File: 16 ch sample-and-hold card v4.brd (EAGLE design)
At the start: 77.2 x 24.8 mm, 33 parts, among them IC1 TL074D, IC2 TL074D, IC3 TL074D, IC4 TL074D, IC5 DG408DY, IC6 DG408DY

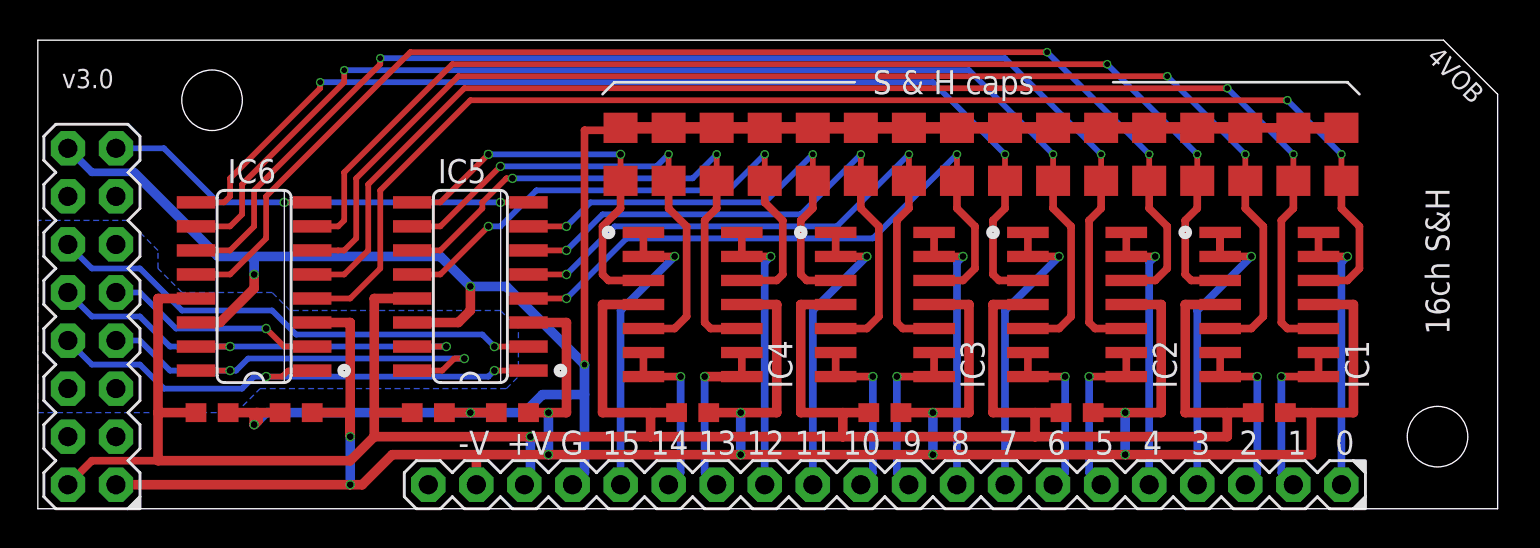
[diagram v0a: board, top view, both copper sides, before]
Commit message: Added new version using 4051 MUX
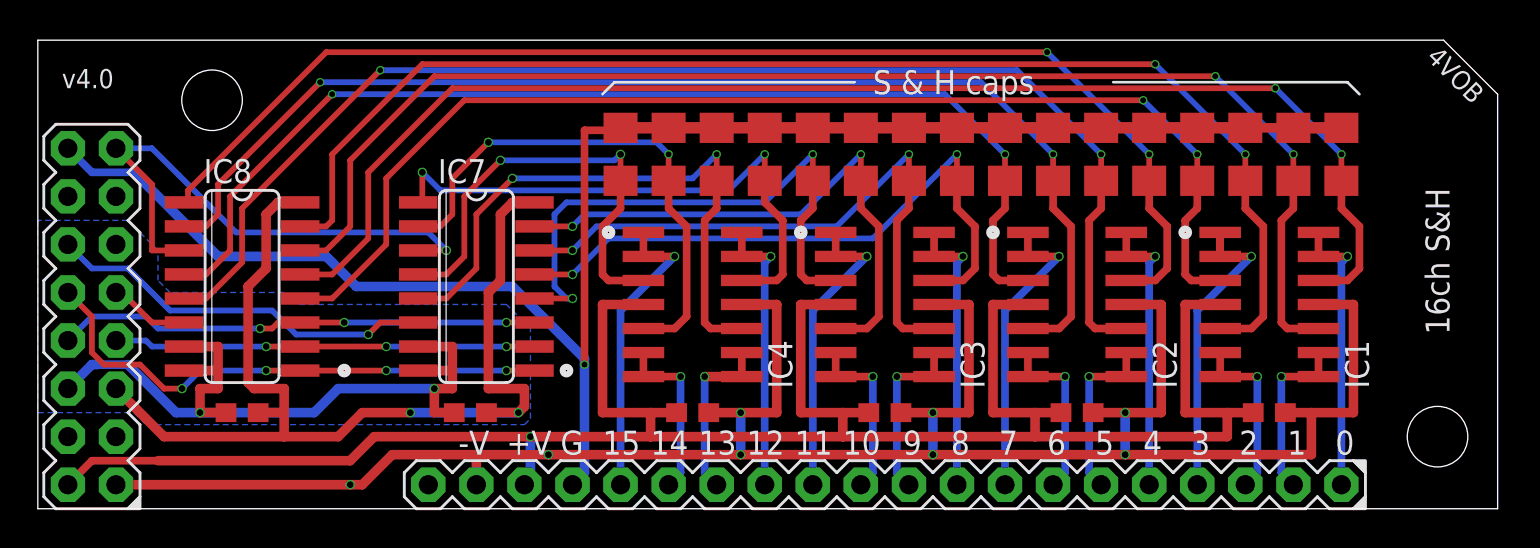
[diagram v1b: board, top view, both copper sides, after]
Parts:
- removed C1, C3: 0.1uF, resistor:C0603
- removed IC5, IC6: DG408DY, maxim:SO16
- added IC7, IC8: 4051D, 40xx:SO16
- moved C2 2.22 mm to (22.5, 5.08), turned to 0 degrees
- moved C40 1.59 mm to (10.5, 5.08), turned to 0 degrees
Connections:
- new net +5V: C2.2, C40.2, IC7.16, IC8.16, SV3.5
- net +15V: no longer C2.2, C40.2, IC5.13, IC6.13
- net -15V: no longer C1.1, C3.1, IC5.3, IC6.3
- net A0: now also IC7.11, IC8.11; no longer IC5.1, IC6.1
- net A1: now also IC7.10, IC8.10; no longer IC5.16, IC6.16
- net A2: now also IC7.9, IC8.9; no longer IC5.15, IC6.15
- net AGND: no longer C1.2, C2.1, C3.2, C40.1, IC5.14, IC6.14
- net DAC: now also IC7.3, IC8.3; no longer IC5.8, IC6.8
- net DGND: now also C2.1, C40.1, IC7.7, IC7.8, IC8.7, IC8.8; no longer SV3.5
- net EN1: now also IC8.6; no longer IC6.2
- net EN2: now also IC7.6; no longer IC5.2
- net IN_0: now also IC8.13; no longer IC6.4
- net IN_1: now also IC8.14; no longer IC6.5
- net IN_10: now also IC7.15; no longer IC5.6
- net IN_11: now also IC7.12; no longer IC5.7
- net IN_12: now also IC7.1; no longer IC5.12
- net IN_13: now also IC7.5; no longer IC5.11
- net IN_14: now also IC7.2; no longer IC5.10
- net IN_15: now also IC7.4; no longer IC5.9
- net IN_2: now also IC8.15; no longer IC6.6
- net IN_3: now also IC8.12; no longer IC6.7
- net IN_4: now also IC8.1; no longer IC6.12
- net IN_5: now also IC8.5; no longer IC6.11
- net IN_6: now also IC8.2; no longer IC6.10
- net IN_7: now also IC8.4; no longer IC6.9
- net IN_8: now also IC7.13; no longer IC5.4
- net IN_9: now also IC7.14; no longer IC5.5
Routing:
- net +5V: track 0.00 -> 56.7 mm, vias 0 -> 2
- net DGND: track 0.00 -> 40.0 mm, vias 0 -> 2
- net AGND: track 126.3 -> 91.3 mm, vias 5 -> 1
- net -15V: track 143.7 -> 118.9 mm, vias 10 -> 8
- net +15V: track 139.2 -> 115.3 mm
- net EN1: track 11.6 -> 4.25 mm, vias 1 -> 0
- net EN2: track 26.6 -> 20.8 mm
- net IN_11: track 25.6 -> 31.0 mm
- net DAC: track 24.5 -> 29.1 mm, vias 2 -> 1
- net A2: track 24.8 -> 28.3 mm, vias 2 -> 4
- net IN_15: track 21.1 -> 24.2 mm
- net A0: track 28.4 -> 25.6 mm, vias 2 -> 3
- net IN_7: track 56.3 -> 58.9 mm
- net IN_13: track 29.8 -> 32.0 mm
- net A1: track 24.2 -> 22.3 mm, vias 2 -> 3
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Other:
- board text added: "v4.0"
- board text removed: "DGND"
- board text removed: "v3.0"

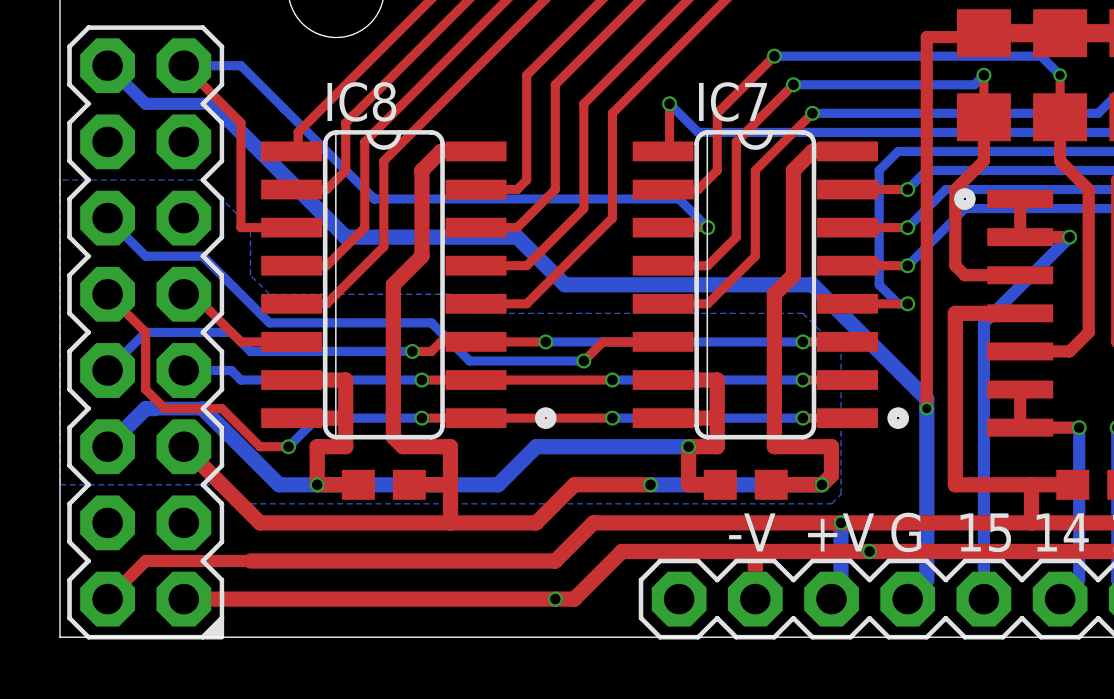
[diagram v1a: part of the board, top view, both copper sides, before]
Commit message: Added 5v reg for muxes directly on board
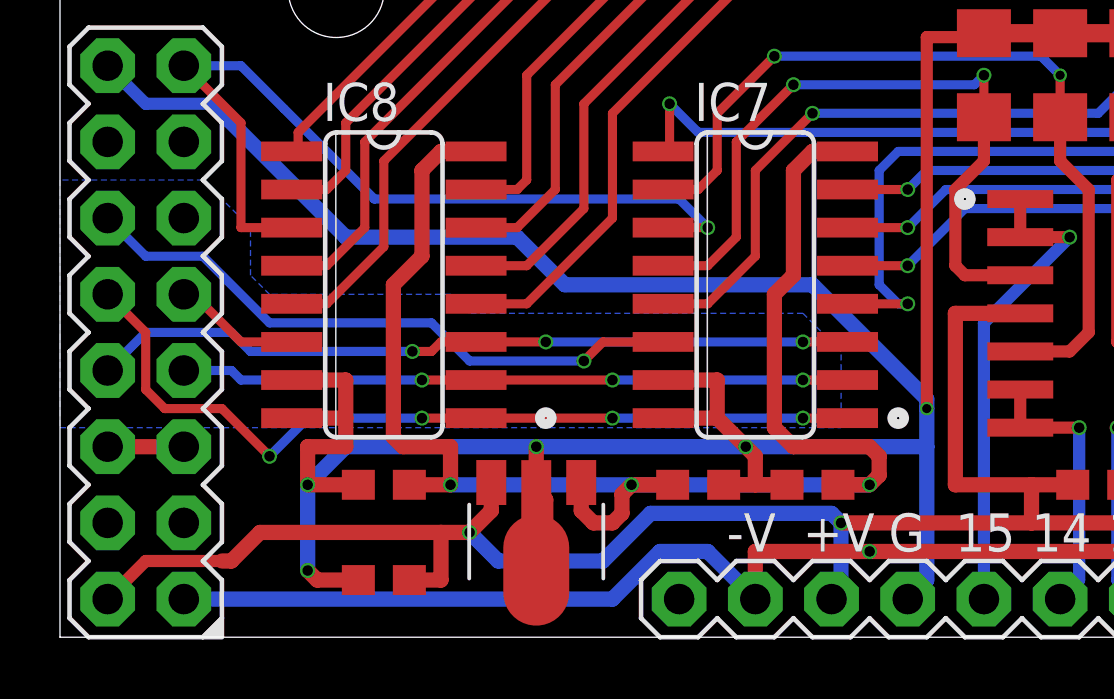
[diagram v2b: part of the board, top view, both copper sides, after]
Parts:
- added C1: 0.1uF, resistor:C0603
- added C3: 0.33uF, resistor:C0603
- added IC5: 78L05F, linear:SOT89
- moved C2 2.22 mm to (24.8, 5.08)
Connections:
- net +15V: now also C3.2, IC5.3
- net +5V: now also C1.2, IC5.1; no longer SV3.5
- net AGND: now also C1.1, C2.1, C3.1, C40.1, IC5.2, IC5.2@1, IC7.7, IC7.8, IC8.7, IC8.8
- net DGND: now also SV3.5; no longer C2.1, C40.1, IC7.7, IC7.8, IC8.7, IC8.8
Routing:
- net AGND: track 91.3 -> 142.6 mm, vias 1 -> 5
- net DGND: track 40.0 -> 2.54 mm, vias 2 -> 0
- net +15V: track 115.3 -> 121.0 mm, vias 1 -> 2
- net +5V: track 56.7 -> 52.0 mm, vias 2 -> 3
- net -15V: track 118.9 -> 119.6 mm, vias 8 -> 7
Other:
- board text added: "DGND"

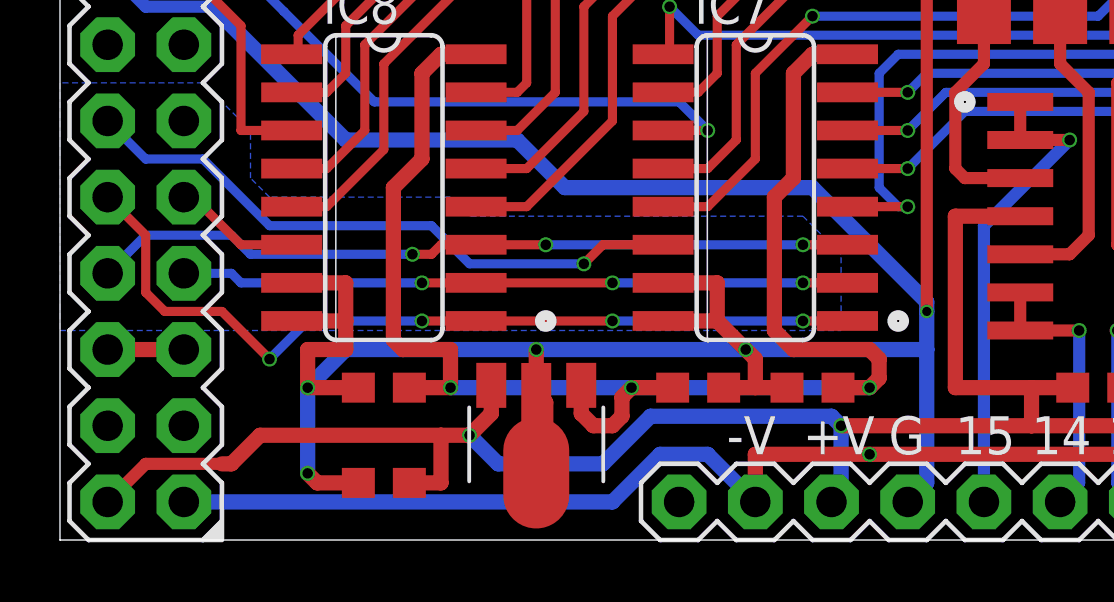
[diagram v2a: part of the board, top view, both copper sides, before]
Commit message: Added selectable agnd/dgnd
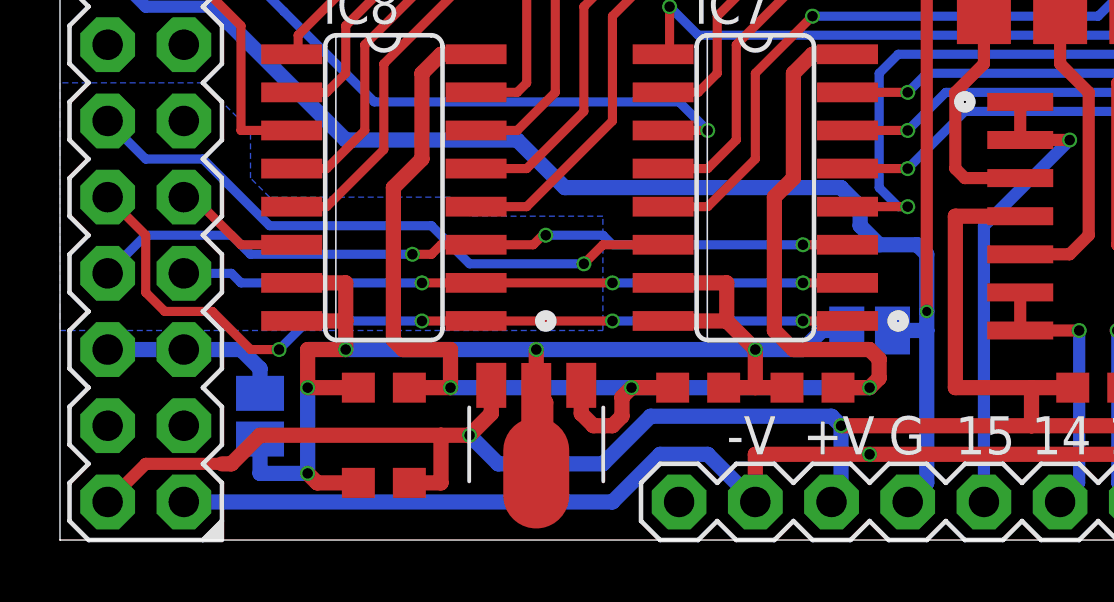
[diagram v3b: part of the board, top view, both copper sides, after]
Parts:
- added SJ1, SJ2: (no value), jumper:SJ
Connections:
- new net N$2: C1.1, C2.1, C3.1, C40.1, IC5.2, IC5.2@1, IC7.7, IC7.8, IC8.7, IC8.8, SJ1.1, SJ2.2
- net AGND: now also SJ1.2; no longer C1.1, C2.1, C3.1, C40.1, IC5.2, IC5.2@1, IC7.7, IC7.8, IC8.7, IC8.8
- net DGND: now also SJ2.1
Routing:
- net N$2: track 0.00 -> 50.3 mm, vias 0 -> 5
- net AGND: track 142.6 -> 93.7 mm, vias 5 -> 1
- net DGND: track 2.54 -> 6.17 mm
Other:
- board text added: "AGND"

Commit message: Added two wires for separate DAC channels to each mux on the SH board
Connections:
- removed net DAC: IC7.3, IC8.3, SV3.15
- new net DAC1: IC8.3, SV3.13
- new net DAC2: IC7.3, SV3.15
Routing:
- net DAC: track 29.1 -> 0.00 mm, vias 1 -> 0
- net DAC2: track 0.00 -> 21.2 mm, vias 0 -> 1
- net DAC1: track 0.00 -> 5.15 mm
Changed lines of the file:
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@@
 <wire x1="13.5509" y1="7.3025" x2="18.0975" y2="7.3025" width="0.3048" layer="1"/>
 </signal>
-<signal name="DAC">
+<signal name="DAC2">
 <via x="21.2725" y="13.6525" extent="1-16" drill="0.35"/>
-<wire x1="21.2725" y1="13.6525" x2="20.32" y2="14.605" width="0.3048" layer="16"/>
-<wire x1="20.32" y1="14.605" x2="10.16" y2="14.605" width="0.3048" layer="16"/>
-<wire x1="10.16" y1="14.605" x2="7.14375" y2="17.62125" width="0.3048" layer="16"/>
+<wire x1="21.2725" y1="13.6525" x2="17.4625" y2="17.4625" width="0.3048" layer="16"/>
+<wire x1="17.4625" y1="17.4625" x2="7.3025" y2="17.4625" width="0.3048" layer="16"/>
 <contactref element="SV3" pad="15"/>
-<wire x1="7.14375" y1="17.62125" x2="5.715" y2="19.05" width="0.3048" layer="16"/>
+<wire x1="7.3025" y1="17.4625" x2="5.715" y2="19.05" width="0.3048" layer="16"/>
 <wire x1="5.715" y1="19.05" x2="3.81" y2="19.05" width="0.3048" layer="16"/>
 <contactref element="IC7" pad="3"/>
-<contactref element="IC8" pad="3"/>
-<wire x1="7.4041" y1="13.6525" x2="5.715" y2="13.6525" width="0.3048" layer="1"/>
-<wire x1="5.715" y1="17.145" x2="3.81" y2="19.05" width="0.3048" layer="1"/>
-<wire x1="5.715" y1="13.6525" x2="5.715" y2="17.145" width="0.3048" layer="1"/>
 <wire x1="21.2725" y1="13.6525" x2="19.7866" y2="13.6525" width="0.3048" layer="1"/>
 </signal>
@@
 <vertex x="12.7" y="11.43"/>
 <vertex x="6.6675" y="11.43"/>
-<vertex x="6.0325" y="12.065"/>
-<vertex x="6.0325" y="13.6525"/>
-<vertex x="4.445" y="15.24"/>
+<vertex x="2.8575" y="15.24"/>
 <vertex x="-0.3175" y="15.24"/>
 </polygon>
@@
 <wire x1="25.0825" y1="6.985" x2="24.4475" y2="6.35" width="0.508" layer="16"/>
 </signal>
+<signal name="DAC1">
+<contactref element="SV3" pad="13"/>
+<contactref element="IC8" pad="3"/>
+<wire x1="3.81" y1="16.51" x2="5.715" y2="14.605" width="0.3048" layer="1"/>
+<wire x1="5.715" y1="13.97" x2="6.0325" y2="13.6525" width="0.3048" layer="1"/>
+<wire x1="6.0325" y1="13.6525" x2="7.4041" y2="13.6525" width="0.3048" layer="1"/>
+<wire x1="5.715" y1="14.605" x2="5.715" y2="13.97" width="0.3048" layer="1"/>
+</signal>
 </signals>
